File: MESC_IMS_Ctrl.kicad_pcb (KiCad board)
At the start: 2 copper layers, 100 x 75 mm, 194 parts, among them J1 Conn_01x08_Female, J10 Conn_01x04_Male, J2 Conn_01x08_Female, J3 Conn_01x08_Female, J4 Conn_01x06_Male, J5 Conn_ARM_JTAG_SWD_10, J6 USB_C_Receptacle_USB2.0, J7 Conn_01x03_Male, J8 Conn_01x04_Male, J9 Conn_01x08_Male, U1 STM32F303CBTx, U10 TPS61041DBV, U2 LM5017MR, U3 TPS76333, U4 INA240A1PW, U5 UCC21520DW, U6 INA240A1PW, U7 UCC21520DW, U8 INA240A1PW, U9 UCC21520DW, Y1 ASE-8.000MHZ-LC-T

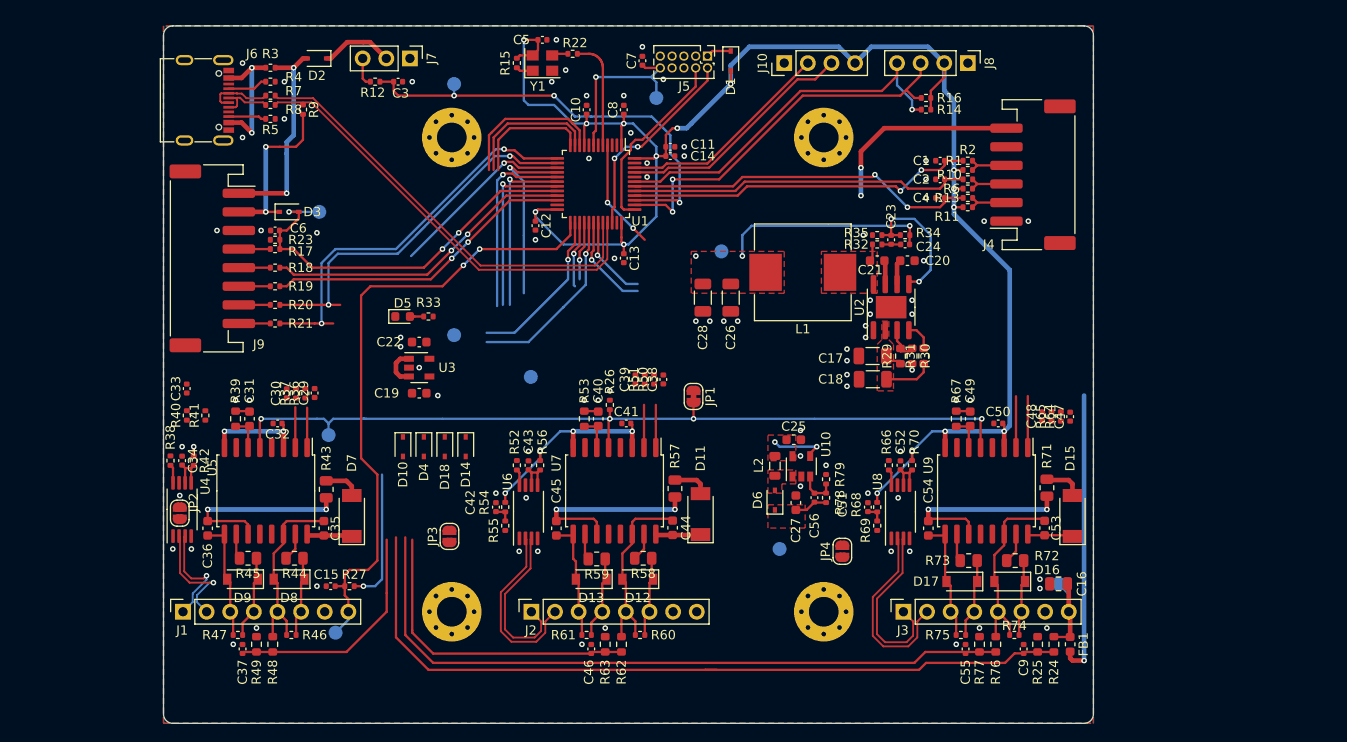
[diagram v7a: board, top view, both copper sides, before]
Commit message: Routing 3V3 reg
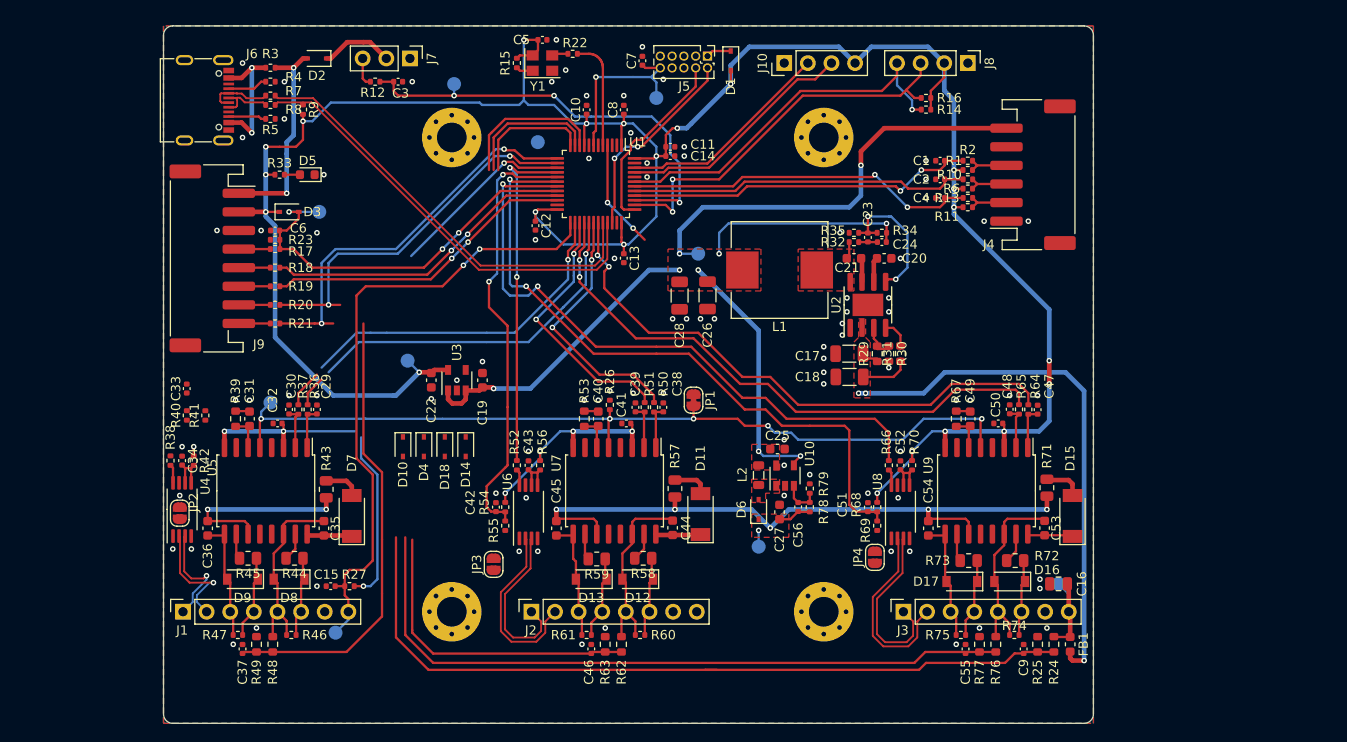
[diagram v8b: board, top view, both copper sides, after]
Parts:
- moved TP2 25.3 mm to (149.2, 87.5)
- moved R33 22.1 mm to (121.5, 91.0), turned to 0 degrees
- moved D5 18.4 mm to (124.5, 91.0), turned to 180 degrees
- moved TP5 7.16 mm to (120.5, 115.5)
- moved C19 6.94 mm to (143.3, 113.1), turned to 90 degrees
- moved TP8 5.71 mm to (135.2, 111.0)
- moved JP3 5.62 mm to (144.5, 132.9)
- moved C22 4.30 mm to (137.8, 113.1), turned to 270 degrees
- moved U3 4.27 mm to (140.6, 113.1), turned to 90 degrees
- moved C47 3.58 mm to (203.0, 116.3)
- moved C48 3.58 mm to (200.0, 116.2)
- moved R64 3.58 mm to (202.0, 116.2)
- moved R65 3.58 mm to (201.0, 116.2)
- moved JP4 3.56 mm to (185.5, 132.2)
- moved C38 3.00 mm to (162.8, 116.0)
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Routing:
- net +3V3: track 252.5 -> 334.0 mm, vias 25 -> 30
- net +5V: track 77.1 -> 153.5 mm, vias 9 -> 11
- net /W_IN_LO: track 6.29 -> 62.0 mm, vias 1 -> 2
- net /W_IN_HI: track 9.15 -> 61.2 mm, vias 1 -> 2
- net /ISW_MCU: track 20.7 -> 71.8 mm, vias 1 -> 2
- net /W_I_SEN: track 18.9 -> 69.1 mm, vias 1 -> 2
- net VDD: track 66.6 -> 97.3 mm, vias 6 -> 8
- net /PSUs/VCC: track 38.1 -> 64.6 mm, vias 1 -> 3
- net /ISV_MCU: track 22.4 -> 47.4 mm, vias 1 -> 2
- net /U_V_SEN: track 68.1 -> 92.0 mm
- net /U_IN_LO: track 17.5 -> 40.9 mm
- net /U_IN_HI: track 20.0 -> 41.7 mm
- net /V_IN_LO: track 7.15 -> 28.2 mm, vias 1 -> 2
- net /V_I_SEN: track 19.4 -> 37.1 mm, vias 1 -> 2
- net /V_IN_HI: track 10.4 -> 27.8 mm, vias 1 -> 2
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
